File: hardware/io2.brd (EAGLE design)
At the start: 98.1 x 60.3 mm, 25 parts, among them IC1 PCF8574T, Q1 BC857BSMD, Q2 BSS123, Q3 BSS123

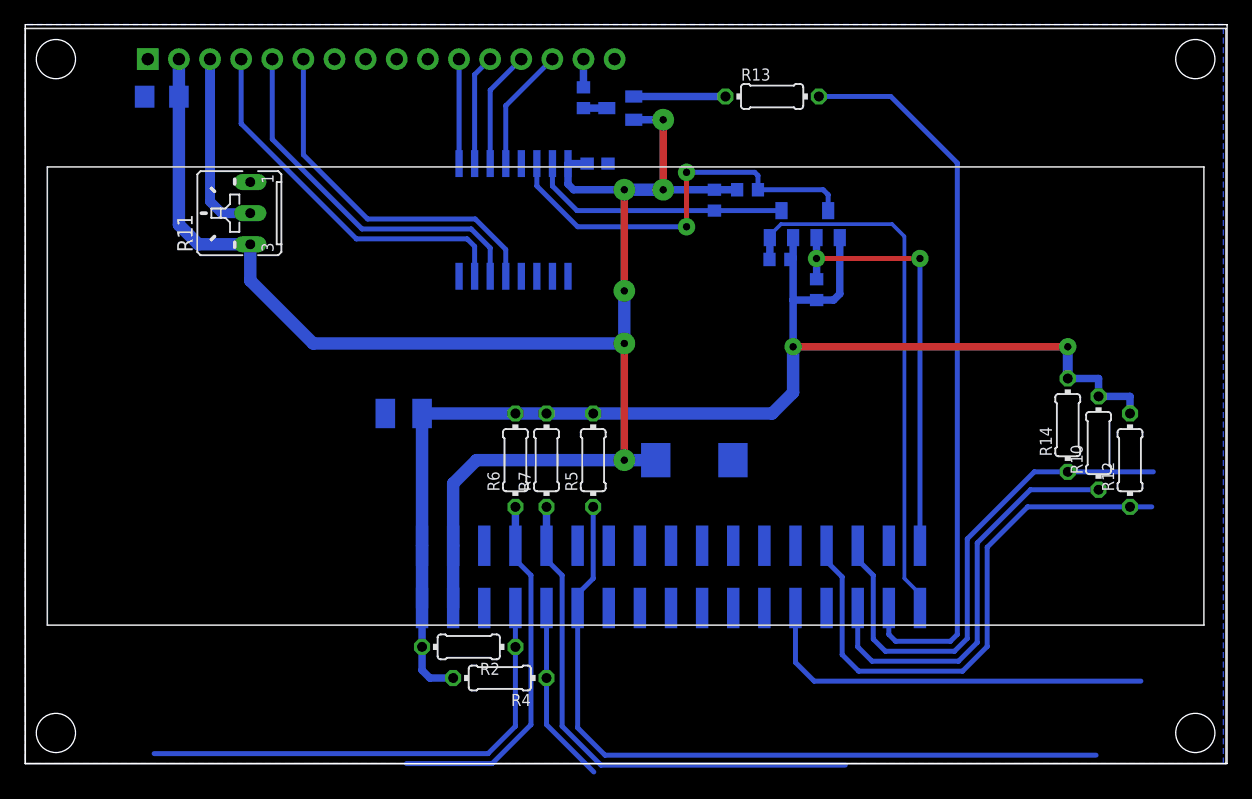
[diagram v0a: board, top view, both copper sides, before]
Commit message: Rotary encoder debounce
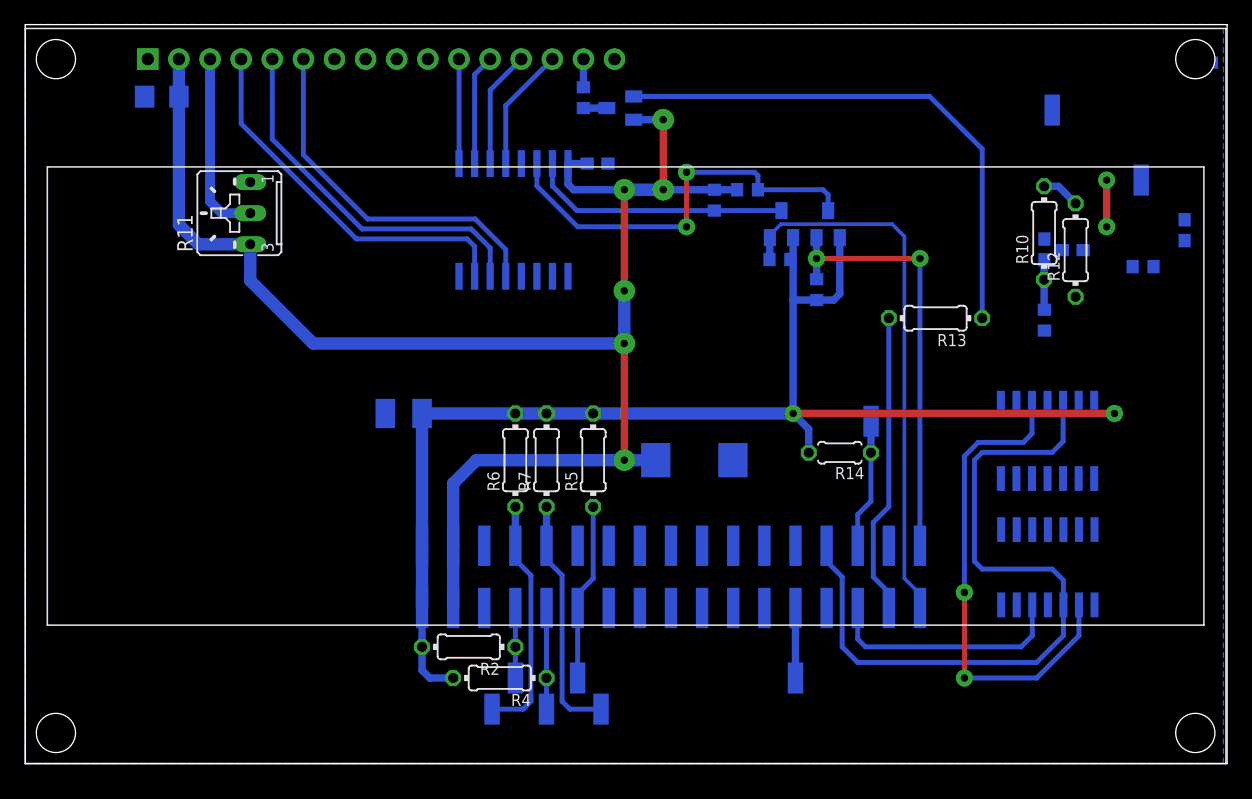
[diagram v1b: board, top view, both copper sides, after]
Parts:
- added C5, C6, C7, C8: (no value), rcl:C0603
- added IC2: 74HC14D, 74xx-eu:SO14
- added IC3: 74HC74D, 74xx-eu:SO14
- added PAD1, PAD2, PAD3, PAD4, PAD5, PAD6, PAD7, PAD8, PAD9: (no value), wirepad:SMD1,27-2,54
- added R16, R17: (no value), rcl:R0603
- R14: device rcl:0204/7 -> rcl:0204/5
- moved R13 22.5 mm to (74.3, 36.4), turned to 180 degrees
- moved R14 18.7 mm to (66.5, 25.4), turned to 180 degrees
- moved R10 17.7 mm to (83.2, 43.3)
- moved R12 17.7 mm to (85.7, 41.9)
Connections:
- new net N$5: PAD8.1, R16.2
- new net N$7: PAD1.1, R17.1
- new net ROT_B_: IC2.10, IC3.2
- new net ROT_DIR: IC3.5, JP1.5
- new net ROT_STEP: IC2.12, IC3.3, JP1.8
- net 3V: now also C7.1, C8.1, IC2.14, IC3.14
- net GND: now also C5.2, C6.2, C7.2, C8.2, IC2.1, IC2.3, IC2.5, IC2.7, IC2.9, IC3.1, IC3.10, IC3.11, IC3.12, IC3.13, IC3.4, IC3.7
- net IR_DATA: now also PAD7.1
- net ROT_A_DT: now also C5.1, IC2.13, R16.1; no longer JP1.5
- net ROT_B_CLK: now also C6.1, IC2.11, R17.2; no longer JP1.8
- net ROT_SW: now also PAD9.1
- net S1: now also PAD4.1
- net S2: now also PAD2.1
- net S3: now also PAD5.1
- net S4: now also PAD3.1
- net S5: now also PAD6.1
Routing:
- net ROT_STEP: track 0.00 -> 59.9 mm
- net S5: track 61.8 -> 14.5 mm
- net ROT_B_CLK: track 45.5 -> 0.02 mm
- net ROT_B_: track 0.00 -> 40.2 mm, vias 0 -> 2
- net N$6: track 7.49 -> 44.0 mm
- net BACKLIGHT: track 60.2 -> 24.7 mm
- net S1: track 40.1 -> 5.71 mm
- net ROT_SW: track 42.2 -> 10.6 mm
- net ROT_A_DT: track 33.9 -> 4.09 mm
- net IR_DATA: track 33.3 -> 5.71 mm
- net S4: track 42.9 -> 19.8 mm
- net ROT_DIR: track 0.00 -> 19.9 mm
- net S2: track 29.8 -> 19.8 mm
- net S3: track 15.0 -> 8.25 mm
- net GND: track 0.00 -> 3.81 mm, vias 0 -> 2
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
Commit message: some changes
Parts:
- moved C8 28.5 mm to (89.7, 29.4)
- moved C7 23.2 mm to (89.8, 19.1), turned to 180 degrees
- moved C6 17.3 mm to (81.0, 32.9), turned to 0 degrees
- moved PAD8 12.2 mm to (86.0, 41.3)
- moved R10 10.1 mm to (89.8, 35.7), turned to 0 degrees
- moved PAD1 9.92 mm to (83.4, 41.3)
- moved R12 9.14 mm to (87.2, 32.9), turned to 0 degrees
- moved C5 8.21 mm to (88.4, 35.7), turned to 180 degrees
- moved R17 8.19 mm to (83.4, 38.1), turned to 270 degrees
- moved R16 3.37 mm to (86.0, 38.1), turned to 90 degrees
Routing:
- net 3V: track 110.4 -> 134.3 mm
- net ROT_B_CLK: track 0.02 -> 9.43 mm
- net ROT_A_DT: track 4.09 -> 9.43 mm
- net GND: track 3.81 -> 0.00 mm, vias 2 -> 0
- net N$7: track 0.00 -> 2.38 mm
- net N$5: track 0.00 -> 2.38 mm
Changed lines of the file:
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@@
 <element name="R6" library="rcl" package="0204/7" value="" x="40.005" y="24.765" rot="R90"/>
 <element name="R7" library="rcl" package="0204/7" value="" x="42.545" y="24.765" rot="R90"/>
-<element name="R10" library="rcl" package="0204/7" value="" x="83.1596" y="43.307" rot="R90"/>
-<element name="R12" library="rcl" package="0204/7" value="" x="85.725" y="41.91" rot="R90"/>
+<element name="R10" library="rcl" package="0204/7" value="" x="89.789" y="35.6616"/>
+<element name="R12" library="rcl" package="0204/7" value="" x="87.249" y="32.893"/>
 <element name="R14" library="rcl" package="0204/5" value="" x="66.4845" y="25.3746" rot="R180"/>
 <element name="C1" library="rcl" package="C0603" value="" x="46.7106" y="48.9712" rot="MR180"/>
@@
 <element name="PAD7" library="wirepad" package="SMD1,27-2,54" value="" x="62.865" y="6.985" rot="MR180"/>
 <element name="PAD9" library="wirepad" package="SMD1,27-2,54" value="" x="69.0372" y="27.94" rot="MR180"/>
-<element name="C5" library="rcl" package="C0603" value="" x="83.185" y="41.9608" rot="MR90"/>
-<element name="C6" library="rcl" package="C0603" value="" x="94.6268" y="43.5356" rot="MR270"/>
-<element name="R16" library="rcl" package="R0603" value="" x="83.185" y="36.195" rot="MR270"/>
-<element name="R17" library="rcl" package="R0603" value="" x="91.2368" y="40.5638" rot="MR180"/>
+<element name="C5" library="rcl" package="C0603" value="" x="88.4428" y="35.6616" rot="MR180"/>
+<element name="C6" library="rcl" package="C0603" value="" x="80.9752" y="32.893" rot="MR0"/>
+<element name="R16" library="rcl" package="R0603" value="" x="85.979" y="38.0746" rot="MR90"/>
+<element name="R17" library="rcl" package="R0603" value="" x="83.439" y="38.0746" rot="MR270"/>
 <element name="IC2" library="74xx-eu" package="SO14" value="74HC14D" x="83.439" y="26.3398" rot="MR0"/>
-<element name="C7" library="rcl" package="C0603" value="" x="85.4964" y="41.91" rot="MR0"/>
+<element name="C7" library="rcl" package="C0603" value="" x="89.7636" y="19.1008" rot="MR180"/>
 <element name="IC3" library="74xx-eu" package="SO14" value="74HC74D" x="83.4644" y="16.0274" rot="MR0"/>
-<element name="C8" library="rcl" package="C0603" value="" x="95.9612" y="57.2008" rot="MR180"/>
-<element name="PAD1" library="wirepad" package="SMD1,27-2,54" value="" x="91.0844" y="47.625" rot="MR0"/>
-<element name="PAD8" library="wirepad" package="SMD1,27-2,54" value="" x="83.82" y="53.34" rot="MR0"/>
+<element name="C8" library="rcl" package="C0603" value="" x="89.7382" y="29.4132" rot="MR180"/>
+<element name="PAD1" library="wirepad" package="SMD1,27-2,54" value="" x="83.439" y="41.3004" rot="MR0"/>
+<element name="PAD8" library="wirepad" package="SMD1,27-2,54" value="" x="85.979" y="41.3004" rot="MR0"/>
 </elements>
 <signals>
@@
 <contactref element="IC2" pad="3"/>
 <contactref element="IC2" pad="1"/>
-<via x="88.265" y="47.625" extent="1-16" drill="0.6" diameter="1.4224" shape="octagon"/>
-<via x="88.265" y="43.815" extent="1-16" drill="0.6" diameter="1.4224" shape="octagon"/>
-<wire x1="88.265" y1="43.815" x2="88.265" y2="47.625" width="0.6096" layer="1"/>
 <contactref element="C7" pad="2"/>
 <contactref element="IC3" pad="7"/>
@@
 <contactref element="IC3" pad="12"/>
 <contactref element="C8" pad="2"/>
-<wire x1="88.265" y1="47.625" x2="96.8112" y2="57.2008" width="0" layer="19" extent="16-16"/>
 </signal>
 <signal name="D4">
@@
 <contactref element="R10" pad="2"/>
 <contactref element="R14" pad="2"/>
-<via x="62.672" y="28.575" extent="1-16" drill="0.6" diameter="1.4224" shape="octagon"/>
 <contactref element="R7" pad="2"/>
 <contactref element="R5" pad="2"/>
@@
 <wire x1="32.385" y1="7.62" x2="33.02" y2="6.985" width="0.6096" layer="16"/>
 <wire x1="33.02" y1="6.985" x2="34.925" y2="6.985" width="0.6096" layer="16"/>
-<via x="88.9" y="28.575" extent="1-16" drill="0.6" diameter="1.4224" shape="octagon"/>
-<wire x1="62.672" y1="28.575" x2="88.9" y2="28.575" width="0.6096" layer="1"/>
+<via x="90.6526" y="23.2156" extent="1-16" drill="0.6" diameter="1.4224" shape="octagon"/>
+<wire x1="63.9572" y1="23.2156" x2="90.6526" y2="23.2156" width="0.6096" layer="1"/>
 <contactref element="C3" pad="+"/>
 <wire x1="32.385" y1="28.5736" x2="32.3864" y2="28.575" width="1.016" layer="16"/>
@@
 <wire x1="46.355" y1="28.575" x2="62.672" y2="28.575" width="1.016" layer="16"/>
 <wire x1="62.672" y1="28.575" x2="62.672" y2="37.8342" width="0.6096" layer="16"/>
-<wire x1="83.1596" y1="47.117" x2="84.328" y2="47.117" width="0.6096" layer="16"/>
-<wire x1="84.328" y1="47.117" x2="85.725" y2="45.72" width="0.6096" layer="16"/>
 <contactref element="IC2" pad="14"/>
 <contactref element="C7" pad="1"/>
 <contactref element="IC3" pad="14"/>
 <contactref element="C8" pad="1"/>
-<wire x1="62.6745" y1="28.5725" x2="62.672" y2="28.575" width="0.6096" layer="16"/>
-<wire x1="63.9445" y1="25.3746" x2="63.9445" y2="27.3025" width="0.6096" layer="16"/>
-<wire x1="63.9445" y1="27.3025" x2="62.672" y2="28.575" width="0.6096" layer="16"/>
-<wire x1="84.328" y1="47.117" x2="95.1112" y2="57.2008" width="0" layer="19" extent="16-16"/>
-<wire x1="86.3464" y1="41.91" x2="85.725" y2="45.72" width="0" layer="19" extent="16-16"/>
-<wire x1="87.249" y1="29.4132" x2="86.3464" y2="41.91" width="0" layer="19" extent="16-16"/>
-<wire x1="88.9" y1="28.575" x2="87.249" y2="29.4132" width="0" layer="19" extent="16-16"/>
-<wire x1="87.2744" y1="19.1008" x2="88.9" y2="28.575" width="0" layer="19" extent="16-16"/>
+<wire x1="63.9445" y1="25.3746" x2="63.9445" y2="27.3025" width="1.016" layer="16"/>
+<wire x1="63.9445" y1="27.3025" x2="62.672" y2="28.575" width="1.016" layer="16"/>
+<wire x1="87.2744" y1="19.1008" x2="88.9136" y2="19.1008" width="0.6096" layer="16"/>
+<wire x1="88.9136" y1="19.1008" x2="88.9136" y2="23.2156" width="0.6096" layer="16"/>
+<wire x1="88.9136" y1="23.495" x2="88.9136" y2="29.3878" width="0.6096" layer="16"/>
+<wire x1="88.9136" y1="29.3878" x2="88.8882" y2="29.4132" width="0.6096" layer="16"/>
+<wire x1="88.8882" y1="29.4132" x2="87.249" y2="29.4132" width="0.6096" layer="16"/>
+<wire x1="88.8882" y1="29.4132" x2="88.8882" y2="30.7222" width="0.6096" layer="16"/>
+<wire x1="88.8882" y1="30.7222" x2="91.059" y2="32.893" width="0.6096" layer="16"/>
+<wire x1="91.059" y1="32.893" x2="91.059" y2="34.544" width="0.6096" layer="16"/>
+<wire x1="91.059" y1="34.544" x2="92.1766" y2="35.6616" width="0.6096" layer="16"/>
+<wire x1="93.599" y1="35.6616" x2="92.1766" y2="35.6616" width="0.6096" layer="16"/>
+<via x="63.9572" y="23.2156" extent="1-16" drill="0.6" diameter="1.4224" shape="octagon"/>
+<wire x1="63.9572" y1="23.2156" x2="63.9572" y2="25.3619" width="1.016" layer="16"/>
+<wire x1="63.9572" y1="25.3619" x2="63.9445" y2="25.3746" width="1.016" layer="16"/>
+<wire x1="90.6526" y1="23.2156" x2="88.9136" y2="23.2156" width="0.6096" layer="16"/>
+<wire x1="88.9136" y1="23.2156" x2="88.9136" y2="23.495" width="0.6096" layer="16"/>
 </signal>
 <signal name="BACKLIGHT">
@@
 <contactref element="C6" pad="1"/>
 <contactref element="R17" pad="2"/>
-<wire x1="85.7368" y1="38.0882" x2="85.725" y2="38.1" width="0.6096" layer="16"/>
 <contactref element="IC2" pad="11"/>
-<wire x1="92.0868" y1="40.5638" x2="94.6268" y2="44.3856" width="0" layer="19" extent="16-16"/>
-<wire x1="85.725" y1="38.1" x2="92.0868" y2="40.5638" width="0" layer="19" extent="16-16"/>
-<wire x1="83.439" y1="29.4132" x2="85.725" y2="38.1" width="0" layer="19" extent="16-16"/>
+<wire x1="83.439" y1="29.4132" x2="83.439" y2="32.893" width="0.6096" layer="16"/>
+<wire x1="81.8252" y1="32.893" x2="83.439" y2="32.893" width="0.6096" layer="16"/>
+<wire x1="83.439" y1="32.893" x2="83.439" y2="37.2246" width="0.6096" layer="16"/>
 </signal>
 <signal name="ROT_A_DT">
 <contactref element="R10" pad="1"/>
 <contactref element="C5" pad="1"/>
-<wire x1="83.1596" y1="39.497" x2="83.1596" y2="41.0854" width="0.6096" layer="16"/>
-<wire x1="83.1596" y1="41.0854" x2="83.185" y2="41.1108" width="0.6096" layer="16"/>
 <contactref element="R16" pad="1"/>
 <contactref element="IC2" pad="13"/>
-<wire x1="83.1596" y1="39.497" x2="83.1596" y2="37.0704" width="0.6096" layer="16"/>
-<wire x1="83.1596" y1="37.0704" x2="83.185" y2="37.045" width="0.6096" layer="16"/>
-<wire x1="85.979" y1="29.4132" x2="83.185" y2="37.045" width="0" layer="19" extent="16-16"/>
+<wire x1="85.979" y1="29.4132" x2="85.979" y2="35.6616" width="0.6096" layer="16"/>
+<wire x1="85.979" y1="35.6616" x2="87.5928" y2="35.6616" width="0.6096" layer="16"/>
+<wire x1="85.979" y1="35.6616" x2="85.979" y2="37.2246" width="0.6096" layer="16"/>
 </signal>
 <signal name="IR_DATA">
@@
 <contactref element="R16" pad="2"/>
 <contactref element="PAD8" pad="1"/>
-<wire x1="83.185" y1="35.345" x2="83.82" y2="53.34" width="0" layer="19" extent="16-16"/>
+<wire x1="85.979" y1="38.9246" x2="85.979" y2="41.3004" width="0.6096" layer="16"/>
 </signal>
 <signal name="N$7">
 <contactref element="R17" pad="1"/>
 <contactref element="PAD1" pad="1"/>
-<wire x1="90.3868" y1="40.5638" x2="91.0844" y2="47.625" width="0" layer="19" extent="16-16"/>
+<wire x1="83.439" y1="38.9246" x2="83.439" y2="41.3004" width="0.6096" layer="16"/>
 </signal>
 <signal name="ROT_DIR">

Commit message: Backlight fixed
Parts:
- R13: device rcl:0204/7 -> rcl:0207/12
- moved R13 20.5 mm to (56.4, 46.4), turned to 270 degrees
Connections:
- net BACKLIGHT: now also IC1.4; no longer JP1.3
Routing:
- net N$6: track 44.0 -> 7.41 mm
- net BACKLIGHT: track 24.7 -> 18.3 mm
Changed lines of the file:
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@@
 <element name="U$1" library="HD44780LCD" package="LCD-20X4-4HOLES" value="LCD-HD447804-HOLES20X4-4HOLES" x="0" y="0"/>
 <element name="R11" library="pot" package="B25U" value="" x="17.4752" y="44.925" rot="R90"/>
-<element name="R13" library="rcl" package="0204/7" value="" x="74.295" y="36.355" rot="R180"/>
+<element name="R13" library="rcl" package="0207/12" value="" x="56.355" y="46.355" rot="R270"/>
 <element name="Q1" library="transistor-pnp" package="SOT23-BEC" value="BC857BSMD" x="48.5648" y="53.5" rot="MR270"/>
 <element name="R9" library="rcl" package="R0603" value="4k7" x="58.9534" y="46.8376" rot="MR0"/>
@@
 <contactref element="Q1" pad="B"/>
 <contactref element="R13" pad="1"/>
-<wire x1="49.6648" y1="54.45" x2="73.82" y2="54.45" width="0.4064" layer="16"/>
-<wire x1="73.82" y1="54.45" x2="76.5175" y2="51.7525" width="0.4064" layer="16"/>
-<wire x1="76.5175" y1="51.7525" x2="76.835" y2="51.435" width="0.4064" layer="16"/>
-<wire x1="78.105" y1="36.355" x2="78.105" y2="50.165" width="0.4064" layer="16"/>
-<wire x1="78.105" y1="50.165" x2="76.835" y2="51.435" width="0.4064" layer="16"/>
+<wire x1="49.6648" y1="54.45" x2="54.61" y2="54.45" width="0.4064" layer="16"/>
+<wire x1="54.61" y1="54.45" x2="56.355" y2="52.705" width="0.4064" layer="16"/>
 </signal>
 <signal name="SDA_3V">
@@
 <via x="48.895" y="34.29" extent="1-16" drill="0.6" diameter="1.778" shape="octagon"/>
 <wire x1="48.895" y1="24.765" x2="48.895" y2="34.29" width="0.6096" layer="1"/>
-<via x="48.895" y="38.5826" extent="1-16" drill="0.6" diameter="1.778" shape="octagon"/>
-<wire x1="48.895" y1="38.5826" x2="48.895" y2="46.8376" width="0.6096" layer="1"/>
-<wire x1="48.895" y1="34.29" x2="48.895" y2="38.5826" width="1.016" layer="16"/>
+<via x="48.895" y="36.6776" extent="1-16" drill="0.6" diameter="1.778" shape="octagon"/>
+<wire x1="48.895" y1="36.6776" x2="48.895" y2="46.8376" width="0.6096" layer="1"/>
+<wire x1="48.895" y1="34.29" x2="48.895" y2="36.6776" width="1.016" layer="16"/>
 <wire x1="48.895" y1="34.29" x2="23.495" y2="34.29" width="1.016" layer="16"/>
 <wire x1="18.3642" y1="39.4208" x2="23.495" y2="34.29" width="1.016" layer="16"/>
@@
 <wire x1="61.7162" y1="45.1367" x2="61.722" y2="45.1309" width="0.4064" layer="16"/>
 <contactref element="IC1" pad="15"/>
-<wire x1="56.2483" y1="45.1367" x2="45.0333" y2="45.1367" width="0.4064" layer="16"/>
-<wire x1="45.0333" y1="45.1367" x2="43.0276" y2="47.1424" width="0.4064" layer="16"/>
+<wire x1="44.2468" y1="45.9232" x2="43.0276" y2="47.1424" width="0.4064" layer="16"/>
 <wire x1="43.0276" y1="48.9738" x2="43.0276" y2="47.1424" width="0.4064" layer="16"/>
+<wire x1="44.2468" y1="45.9232" x2="47.6758" y2="45.9232" width="0.4064" layer="16"/>
+<wire x1="47.6758" y1="45.9232" x2="48.4623" y2="45.1367" width="0.4064" layer="16"/>
+<wire x1="56.2483" y1="45.1367" x2="48.4623" y2="45.1367" width="0.4064" layer="16"/>
 </signal>
 <signal name="SCL_5V">
@@
 <contactref element="IC1" pad="14"/>
 <wire x1="41.7576" y1="48.9738" x2="41.7576" y2="47.1424" width="0.4064" layer="16"/>
-<wire x1="41.7576" y1="47.1424" x2="45.085" y2="43.815" width="0.4064" layer="16"/>
-<wire x1="45.085" y1="43.815" x2="53.975" y2="43.815" width="0.4064" layer="16"/>
+<wire x1="41.7576" y1="47.1424" x2="43.7896" y2="45.1104" width="0.4064" layer="16"/>
 <via x="53.975" y="43.815" extent="1-16" drill="0.6" diameter="1.4224" shape="octagon"/>
 <wire x1="53.975" y1="43.815" x2="53.975" y2="48.26" width="0.4064" layer="1"/>
@@
 <wire x1="65.1256" y1="46.8376" x2="65.532" y2="46.4312" width="0.4064" layer="16"/>
 <wire x1="65.532" y1="45.1309" x2="65.532" y2="46.4312" width="0.4064" layer="16"/>
+<wire x1="43.7896" y1="45.1104" x2="47.3456" y2="45.1104" width="0.4064" layer="16"/>
+<wire x1="47.3456" y1="45.1104" x2="48.641" y2="43.815" width="0.4064" layer="16"/>
+<wire x1="48.641" y1="43.815" x2="53.975" y2="43.815" width="0.4064" layer="16"/>
 </signal>
 <signal name="3V">
@@
 </signal>
 <signal name="BACKLIGHT">
-<contactref element="JP1" pad="3"/>
 <contactref element="R13" pad="2"/>
-<wire x1="70.485" y1="12.7" x2="70.485" y2="13.97" width="0.4064" layer="16"/>
-<wire x1="70.485" y1="13.97" x2="69.215" y2="15.24" width="0.4064" layer="16"/>
-<wire x1="69.215" y1="15.24" x2="69.215" y2="19.685" width="0.4064" layer="16"/>
-<wire x1="69.215" y1="19.685" x2="70.485" y2="20.955" width="0.4064" layer="16"/>
-<wire x1="70.485" y1="20.955" x2="70.485" y2="36.355" width="0.4064" layer="16"/>
+<contactref element="IC1" pad="4"/>
+<wire x1="56.355" y1="40.005" x2="46.99" y2="40.005" width="0.4064" layer="16"/>
+<wire x1="40.4876" y1="39.7738" x2="40.4876" y2="41.1226" width="0.4064" layer="16"/>
+<wire x1="40.4876" y1="41.1226" x2="41.275" y2="41.91" width="0.4064" layer="16"/>
+<wire x1="41.275" y1="41.91" x2="45.085" y2="41.91" width="0.4064" layer="16"/>
+<wire x1="45.085" y1="41.91" x2="46.99" y2="40.005" width="0.4064" layer="16"/>
 </signal>
 <signal name="S1">
